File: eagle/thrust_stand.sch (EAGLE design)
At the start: 27 parts, among them IC1 7805TV, Q1 16Mhz, Q2 IRF510, T1 2N3904, U2 ATMEGA328P_PDIP

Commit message: parts placed
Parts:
- R10: device rcl:R-US_0207/2V -> rcl:R-US_0207/7
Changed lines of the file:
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@@
 <grid distance="0.1" unitdist="inch" unit="inch" style="lines" multiple="1" display="no" altdistance="0.01" altunitdist="inch" altunit="inch"/>
 <layers>
-<layer number="1" name="Top" color="4" fill="1" visible="no" active="no"/>
-<layer number="16" name="Bottom" color="1" fill="1" visible="no" active="no"/>
-<layer number="17" name="Pads" color="2" fill="1" visible="no" active="no"/>
-<layer number="18" name="Vias" color="2" fill="1" visible="no" active="no"/>
-<layer number="19" name="Unrouted" color="6" fill="1" visible="no" active="no"/>
-<layer number="20" name="Dimension" color="15" fill="1" visible="no" active="no"/>
-<layer number="21" name="tPlace" color="7" fill="1" visible="no" active="no"/>
-<layer number="22" name="bPlace" color="7" fill="1" visible="no" active="no"/>
-<layer number="23" name="tOrigins" color="15" fill="1" visible="no" active="no"/>
-<layer number="24" name="bOrigins" color="15" fill="1" visible="no" active="no"/>
-<layer number="25" name="tNames" color="7" fill="1" visible="no" active="no"/>
-<layer number="26" name="bNames" color="7" fill="1" visible="no" active="no"/>
-<layer number="27" name="tValues" color="7" fill="1" visible="no" active="no"/>
-<layer number="28" name="bValues" color="7" fill="1" visible="no" active="no"/>
+<layer number="1" name="Top" color="4" fill="1" visible="yes" active="no"/>
+<layer number="16" name="Bottom" color="1" fill="1" visible="yes" active="no"/>
+<layer number="17" name="Pads" color="2" fill="1" visible="yes" active="no"/>
+<layer number="18" name="Vias" color="2" fill="1" visible="yes" active="no"/>
+<layer number="19" name="Unrouted" color="6" fill="1" visible="yes" active="no"/>
+<layer number="20" name="Dimension" color="15" fill="1" visible="yes" active="no"/>
+<layer number="21" name="tPlace" color="7" fill="1" visible="yes" active="no"/>
+<layer number="22" name="bPlace" color="7" fill="1" visible="yes" active="no"/>
+<layer number="23" name="tOrigins" color="15" fill="1" visible="yes" active="no"/>
+<layer number="24" name="bOrigins" color="15" fill="1" visible="yes" active="no"/>
+<layer number="25" name="tNames" color="7" fill="1" visible="yes" active="no"/>
+<layer number="26" name="bNames" color="7" fill="1" visible="yes" active="no"/>
+<layer number="27" name="tValues" color="7" fill="1" visible="yes" active="no"/>
+<layer number="28" name="bValues" color="7" fill="1" visible="yes" active="no"/>
 <layer number="29" name="tStop" color="7" fill="3" visible="no" active="no"/>
 <layer number="30" name="bStop" color="7" fill="6" visible="no" active="no"/>
@@
 <layer number="35" name="tGlue" color="7" fill="4" visible="no" active="no"/>
 <layer number="36" name="bGlue" color="7" fill="5" visible="no" active="no"/>
-<layer number="37" name="tTest" color="7" fill="1" visible="no" active="no"/>
-<layer number="38" name="bTest" color="7" fill="1" visible="no" active="no"/>
+<layer number="37" name="tTest" color="7" fill="1" visible="yes" active="no"/>
+<layer number="38" name="bTest" color="7" fill="1" visible="yes" active="no"/>
 <layer number="39" name="tKeepout" color="4" fill="11" visible="no" active="no"/>
 <layer number="40" name="bKeepout" color="1" fill="11" visible="no" active="no"/>
@@
 <layer number="44" name="Drills" color="7" fill="1" visible="no" active="no"/>
 <layer number="45" name="Holes" color="7" fill="1" visible="no" active="no"/>
-<layer number="46" name="Milling" color="3" fill="1" visible="no" active="no"/>
-<layer number="47" name="Measures" color="7" fill="1" visible="no" active="no"/>
-<layer number="48" name="Document" color="7" fill="1" visible="no" active="no"/>
-<layer number="49" name="Reference" color="7" fill="1" visible="no" active="no"/>
-<layer number="50" name="dxf" color="7" fill="1" visible="no" active="no"/>
-<layer number="51" name="tDocu" color="7" fill="1" visible="no" active="no"/>
-<layer number="52" name="bDocu" color="7" fill="1" visible="no" active="no"/>
-<layer number="53" name="tGND_GNDA" color="7" fill="9" visible="no" active="no"/>
-<layer number="54" name="bGND_GNDA" color="1" fill="9" visible="no" active="no"/>
-<layer number="56" name="wert" color="7" fill="1" visible="no" active="no"/>
-<layer number="57" name="tCAD" color="7" fill="1" visible="no" active="no"/>
-<layer number="59" name="tCarbon" color="7" fill="1" visible="no" active="no"/>
-<layer number="60" name="bCarbon" color="7" fill="1" visible="no" active="no"/>
+<layer number="46" name="Milling" color="3" fill="1" visible="yes" active="no"/>
+<layer number="47" name="Measures" color="7" fill="1" visible="yes" active="no"/>
+<layer number="48" name="Document" color="7" fill="1" visible="yes" active="no"/>
+<layer number="49" name="Reference" color="7" fill="1" visible="yes" active="no"/>
+<layer number="50" name="dxf" color="7" fill="1" visible="yes" active="no"/>
+<layer number="51" name="tDocu" color="7" fill="1" visible="yes" active="no"/>
+<layer number="52" name="bDocu" color="7" fill="1" visible="yes" active="no"/>
+<layer number="53" name="tGND_GNDA" color="7" fill="9" visible="yes" active="no"/>
+<layer number="54" name="bGND_GNDA" color="1" fill="9" visible="yes" active="no"/>
+<layer number="56" name="wert" color="7" fill="1" visible="yes" active="no"/>
+<layer number="57" name="tCAD" color="7" fill="1" visible="yes" active="no"/>
+<layer number="59" name="tCarbon" color="7" fill="1" visible="yes" active="no"/>
+<layer number="60" name="bCarbon" color="7" fill="1" visible="yes" active="no"/>
 <layer number="90" name="Modules" color="5" fill="1" visible="yes" active="yes"/>
 <layer number="91" name="Nets" color="2" fill="1" visible="yes" active="yes"/>
@@
 <part name="GND9" library="supply1" deviceset="GND" device=""/>
 <part name="R5" library="rcl" deviceset="R-US_" device="0207/7" value="220"/>
-<part name="R10" library="rcl" deviceset="R-US_" device="0207/2V" value="10k"/>
+<part name="R10" library="rcl" deviceset="R-US_" device="0207/7" value="10k"/>
 <part name="GND5" library="supply1" deviceset="GND" device=""/>
 <part name="HX711" library="con-molex" deviceset="22-23-2051" device=""/>

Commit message: tweaks
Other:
- moved on the sheet: BATTERY-1, BATTERY-2, C4, I2C_1-1, I2C_1-2, I2C_1-3, I2C_1-4, I2C_2-1, I2C_2-2, I2C_2-3, I2C_2-4, I2C_3-1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

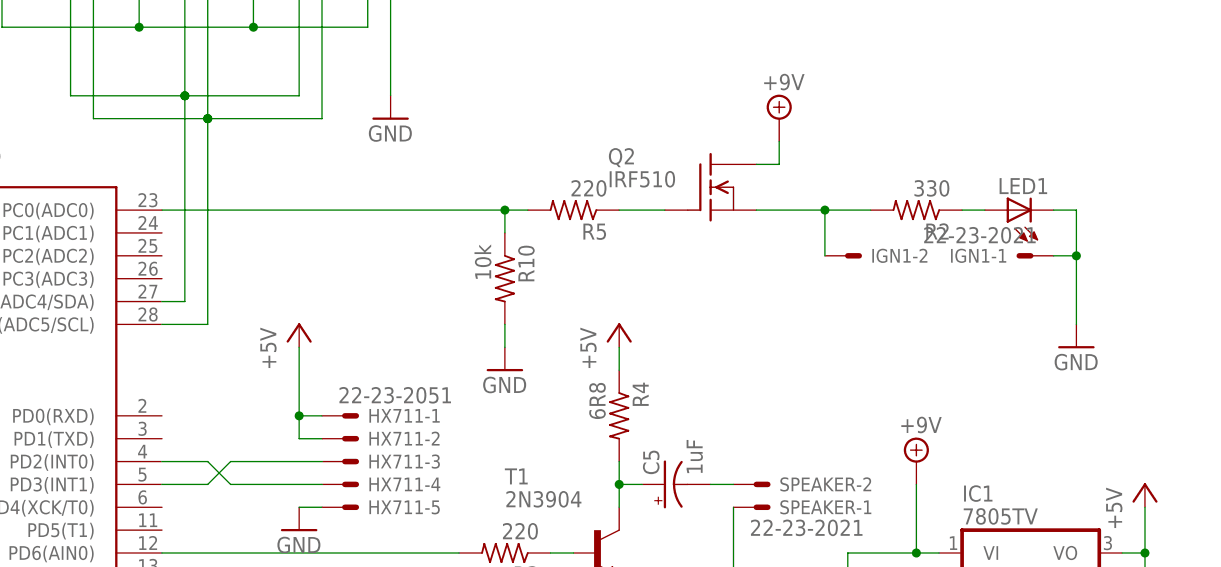
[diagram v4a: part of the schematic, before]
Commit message: larger header for igniter
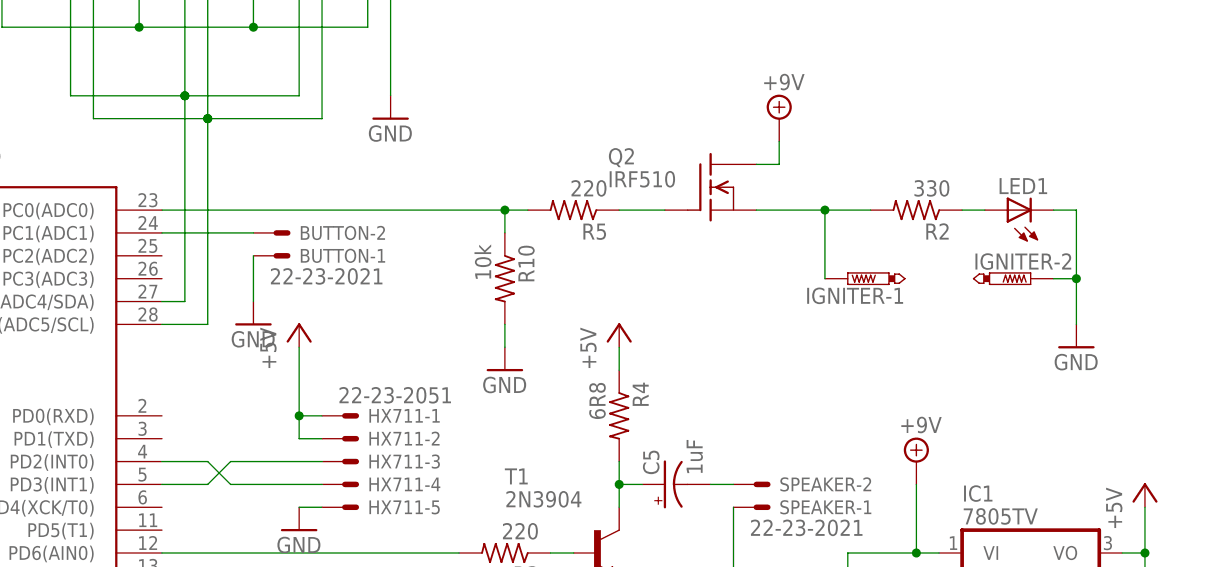
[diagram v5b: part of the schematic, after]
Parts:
- removed IGN1: 22-23-2021, con-molex:22-23-2021
- added BUTTON: 22-23-2021, con-molex:22-23-2021
- added IGNITER: PTR2, testpad:PTR2
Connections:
- new net N$17: BUTTON-2.S, U2.PC1(ADC1)
- net GND: now also BUTTON-1.S, IGNITER-2.TP; no longer IGN1-1.S
- net N$24: now also IGNITER-1.TP; no longer IGN1-2.S
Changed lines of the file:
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@@
 <part name="SUPPLY1" library="supply2" deviceset="+9V" device=""/>
 <part name="R2" library="rcl" deviceset="R-US_" device="0207/7" value="330"/>
-<part name="IGN1" library="con-molex" deviceset="22-23-2021" device=""/>
 <part name="LED1" library="led" deviceset="LED" device="5MM"/>
 <part name="GND6" library="supply1" deviceset="GND" device=""/>
@@
 <part name="GND7" library="supply1" deviceset="GND" device=""/>
 <part name="GND10" library="supply1" deviceset="GND" device=""/>
+<part name="BUTTON" library="con-molex" deviceset="22-23-2021" device=""/>
+<part name="GND11" library="supply1" deviceset="GND" device=""/>
+<part name="IGNITER" library="testpad" deviceset="PTR2" device=""/>
 </parts>
 <sheets>
@@
 <instance part="SUPPLY1" gate="G$1" x="109.22" y="83.82"/>
 <instance part="R2" gate="G$1" x="124.46" y="73.66" rot="R180"/>
-<instance part="IGN1" gate="-1" x="137.16" y="68.58" rot="MR0"/>
-<instance part="IGN1" gate="-2" x="116.84" y="68.58" rot="MR180"/>
 <instance part="LED1" gate="G$1" x="134.62" y="73.66" rot="R90"/>
 <instance part="GND6" gate="1" x="142.24" y="58.42"/>
@@
 <instance part="GND7" gate="1" x="91.44" y="25.4"/>
 <instance part="GND10" gate="1" x="104.14" y="25.4"/>
+<instance part="BUTTON" gate="-1" x="53.34" y="68.58" rot="MR180"/>
+<instance part="BUTTON" gate="-2" x="53.34" y="71.12" rot="MR180"/>
+<instance part="GND11" gate="1" x="50.8" y="60.96"/>
+<instance part="IGNITER" gate="-1" x="116.84" y="66.04" rot="R90"/>
+<instance part="IGNITER" gate="-2" x="137.16" y="66.04" rot="R270"/>
 </instances>
 <busses>
@@
 <pinref part="LED1" gate="G$1" pin="C"/>
 <wire x1="139.7" y1="73.66" x2="142.24" y2="73.66" width="0.1524" layer="91"/>
-<wire x1="142.24" y1="73.66" x2="142.24" y2="68.58" width="0.1524" layer="91"/>
-<pinref part="IGN1" gate="-1" pin="S"/>
-<wire x1="139.7" y1="68.58" x2="142.24" y2="68.58" width="0.1524" layer="91"/>
+<wire x1="142.24" y1="73.66" x2="142.24" y2="66.04" width="0.1524" layer="91"/>
+<wire x1="139.7" y1="66.04" x2="142.24" y2="66.04" width="0.1524" layer="91"/>
 <pinref part="GND6" gate="1" pin="GND"/>
-<wire x1="142.24" y1="68.58" x2="142.24" y2="60.96" width="0.1524" layer="91"/>
-<junction x="142.24" y="68.58"/>
+<wire x1="142.24" y1="66.04" x2="142.24" y2="60.96" width="0.1524" layer="91"/>
+<junction x="142.24" y="66.04"/>
+<pinref part="IGNITER" gate="-2" pin="TP"/>
 </segment>
 <segment>
@@
 <pinref part="GND7" gate="1" pin="GND"/>
 <wire x1="91.44" y1="30.48" x2="91.44" y2="27.94" width="0.1524" layer="91"/>
+</segment>
+<segment>
+<pinref part="GND11" gate="1" pin="GND"/>
+<pinref part="BUTTON" gate="-1" pin="S"/>
+<wire x1="50.8" y1="63.5" x2="50.8" y2="68.58" width="0.1524" layer="91"/>
 </segment>
 </net>
@@
 <pinref part="R2" gate="G$1" pin="2"/>
 <wire x1="106.68" y1="73.66" x2="114.3" y2="73.66" width="0.1524" layer="91"/>
-<pinref part="IGN1" gate="-2" pin="S"/>
 <wire x1="114.3" y1="73.66" x2="119.38" y2="73.66" width="0.1524" layer="91"/>
-<wire x1="114.3" y1="68.58" x2="114.3" y2="73.66" width="0.1524" layer="91"/>
+<wire x1="114.3" y1="66.04" x2="114.3" y2="73.66" width="0.1524" layer="91"/>
 <junction x="114.3" y="73.66"/>
+<pinref part="IGNITER" gate="-1" pin="TP"/>
 </segment>
 </net>
@@
 </segment>
 </net>
+<net name="N$17" class="0">
+<segment>
+<pinref part="BUTTON" gate="-2" pin="S"/>
+<pinref part="U2" gate="G$1" pin="PC1(ADC1)"/>
+<wire x1="50.8" y1="71.12" x2="40.64" y2="71.12" width="0.1524" layer="91"/>
+</segment>
+</net>

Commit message: rotary encoder schemo and codes
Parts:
- added SW1: EC12E_SW, switch-alps:EC12E_SW
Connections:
- new net N$19: SW1G$1.B, U2.PD2(INT0)
- new net N$20: SW1G$1.A, U2.PD3(INT1)
- new net N$22: SW1G$2.1, U2.PD4(XCK/T0)
- net GND: now also SW1G$1.C, SW1G$2.2
- net N$13: now also U2.PD5(T1); no longer U2.PD6(AIN0)
- net N$3: now also U2.PD6(AIN0); no longer U2.PD3(INT1)
- net N$6: now also U2.PD7(AIN1); no longer U2.PD2(INT0)
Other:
- moved on the sheet: HX711-1, HX711-2, HX711-3, HX711-4, HX711-5, R3, SD_CARD-1, SD_CARD-2, SD_CARD-3, SD_CARD-4, SD_CARD-5, SD_CARD-6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
